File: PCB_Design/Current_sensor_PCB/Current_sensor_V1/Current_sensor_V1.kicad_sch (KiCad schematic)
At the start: 24 parts, among them J1 Screw_Terminal_01x02, J2 Barrel_Jack_MountingPin, J3 Conn_Coaxial, J4 Conn_Coaxial, J5 Conn_Coaxial, U1 CASR_6-NP

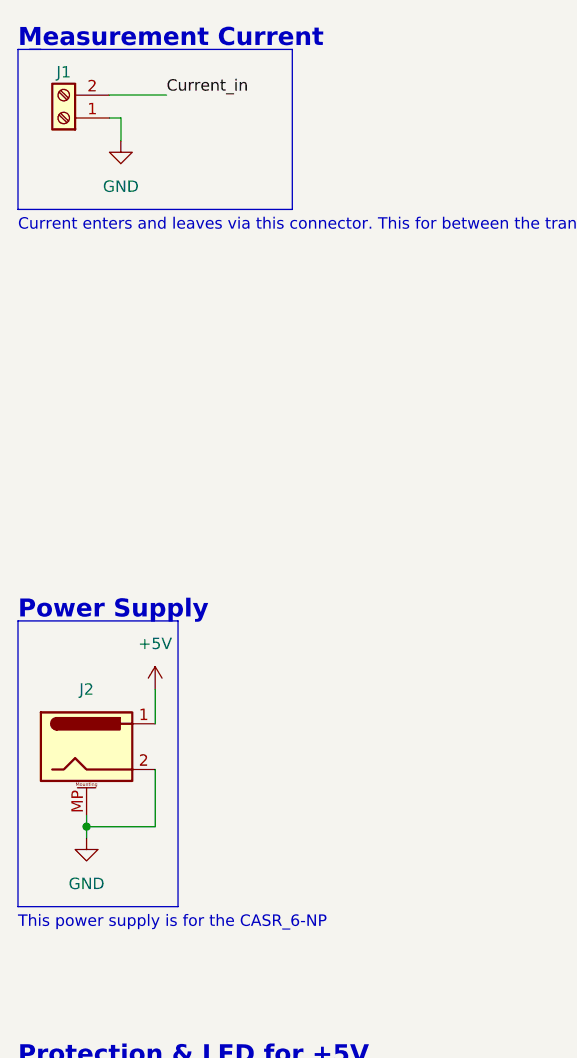
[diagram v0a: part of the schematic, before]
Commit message: Made Footprint and placed everything in the correct spot for Current V1
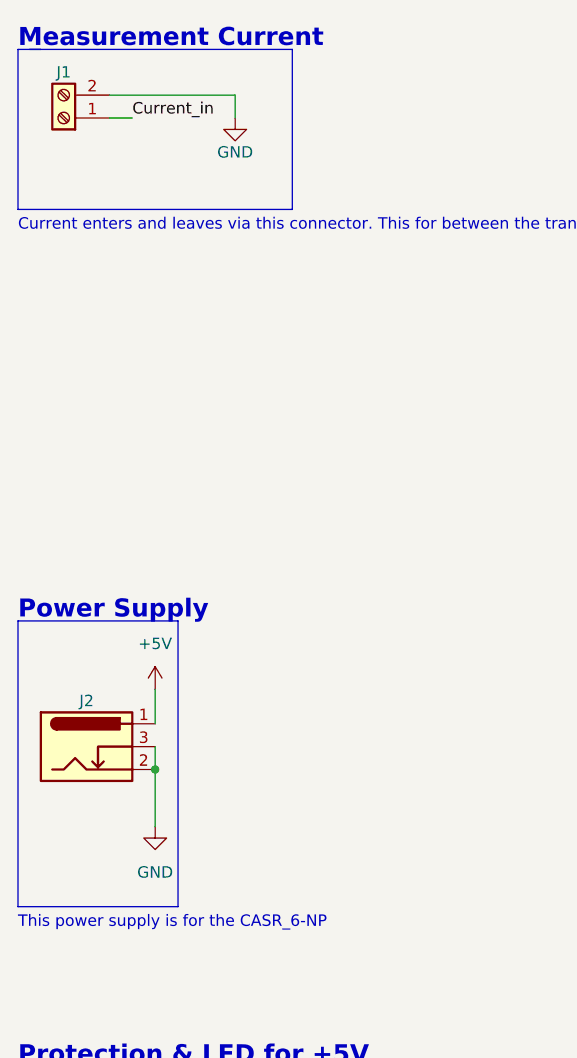
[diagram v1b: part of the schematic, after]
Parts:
- removed J2: Barrel_Jack_MountingPin, Connector_BarrelJack:BarrelJack_CLIFF_FC681465S_SMT_Horizontal, symbol Connector:Barrel_Jack_MountingPin
- added J2: Barrel_Jack_Switch, Connector_BarrelJack:BarrelJack_CLIFF_FC681465S_SMT_Horizontal, symbol Connector:Barrel_Jack_Switch
- J1: footprint (none) -> Custom_library:2_pin_terminal_block_socket
- R2: footprint (none) -> Custom_library:Shunt_Resistor
- U1: footprint (none) -> Custom_library:CASR6NP
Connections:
- net +5V: now also J2.1
- net Current_in: now also J1.1 (Pin_1); no longer J1.2 (Pin_2)
- net GND: now also J1.2 (Pin_2), J2.2, J2.3; no longer J1.1 (Pin_1)
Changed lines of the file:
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@@
   (junction (at 113.03 83.82) (diameter 0) (color 0 0 0 0)
   )
-  (junction (at 21.59 111.76) (diameter 0) (color 0 0 0 0)
-  )
   (junction (at 104.14 100.33) (diameter 0) (color 0 0 0 0)
   )
@@
   (junction (at 85.09 97.79) (diameter 0) (color 0 0 0 0)
   )
+  (junction (at 29.21 105.41) (diameter 0) (color 0 0 0 0)
+  )
   (wire (pts (xy 101.6 88.9) (xy 107.95 88.9))
     (stroke (width 0) (type default) (color 0 0 0 0))
@@
     (stroke (width 0) (type default) (color 0 0 0 0))
   )
-  (wire (pts (xy 25.4 35.56) (xy 25.4 33.02))
+  (wire (pts (xy 38.1 33.02) (xy 38.1 30.48))
     (stroke (width 0) (type default) (color 0 0 0 0))
   )
@@
     (stroke (width 0) (type default) (color 0 0 0 0))
   )
-  (wire (pts (xy 25.4 33.02) (xy 24.13 33.02))
-    (stroke (width 0) (type default) (color 0 0 0 0))
-  )
   (wire (pts (xy 26.67 156.21) (xy 26.67 157.48))
     (stroke (width 0) (type default) (color 0 0 0 0))
@@
     (stroke (width 0) (type default) (color 0 0 0 0))
   )
-  (wire (pts (xy 24.13 30.48) (xy 30.48 30.48))
-    (stroke (width 0) (type default) (color 0 0 0 0))
-  )
   (wire (pts (xy 231.14 97.79) (xy 234.95 97.79))
     (stroke (width 0) (type default) (color 0 0 0 0))
   )
+  (wire (pts (xy 24.13 33.02) (xy 26.67 33.02))
+    (stroke (width 0) (type default) (color 0 0 0 0))
+  )
   (wire (pts (xy 88.9 97.79) (xy 92.71 97.79))
     (stroke (width 0) (type default) (color 0 0 0 0))
@@
     (stroke (width 0) (type default) (color 0 0 0 0))
   )
-  (wire (pts (xy 21.59 110.49) (xy 21.59 111.76))
-    (stroke (width 0) (type default) (color 0 0 0 0))
-  )
   (wire (pts (xy 171.45 97.79) (xy 172.72 97.79))
     (stroke (width 0) (type default) (color 0 0 0 0))
@@
     (stroke (width 0) (type default) (color 0 0 0 0))
   )
+  (wire (pts (xy 24.13 30.48) (xy 38.1 30.48))
+    (stroke (width 0) (type default) (color 0 0 0 0))
+  )
   (wire (pts (xy 172.72 115.57) (xy 175.26 115.57))
     (stroke (width 0) (type default) (color 0 0 0 0))
@@
     (stroke (width 0) (type default) (color 0 0 0 0))
   )
-  (wire (pts (xy 21.59 111.76) (xy 21.59 113.03))
-    (stroke (width 0) (type default) (color 0 0 0 0))
-  )
   (wire (pts (xy 240.03 87.63) (xy 240.03 88.9))
     (stroke (width 0) (type default) (color 0 0 0 0))
@@
     (stroke (width 0) (type default) (color 0 0 0 0))
   )
-  (wire (pts (xy 21.59 111.76) (xy 29.21 111.76))
-    (stroke (width 0) (type default) (color 0 0 0 0))
-  )
   (wire (pts (xy 101.6 74.93) (xy 101.6 76.2))
+    (stroke (width 0) (type default) (color 0 0 0 0))
+  )
+  (wire (pts (xy 29.21 102.87) (xy 29.21 105.41))
     (stroke (width 0) (type default) (color 0 0 0 0))
   )
@@
     (effects (font (size 1.27 1.27)) (justify left bottom))
   )
-  (label "Current_in" (at 30.48 30.48 0)
+  (label "Current_in" (at 26.67 33.02 0)
     (effects (font (size 1.27 1.27)) (justify left bottom))
   )
@@
     (pin "2")
   )
-  (symbol (lib_id "power:GND") (at 25.4 35.56 0) (unit 1)
-    (in_bom yes) (on_board yes) (fields_autoplaced)
-    (property "Reference" "#PWR02" (id 0) (at 25.4 41.91 0)
-      (effects (font (size 1.27 1.27)) hide)
-    )
-    (property "Value" "GND" (id 1) (at 25.4 40.64 0))
-    (property "Footprint" "" (id 2) (at 25.4 35.56 0)
-      (effects (font (size 1.27 1.27)) hide)
-    )
-    (property "Datasheet" "" (id 3) (at 25.4 35.56 0)
+  (symbol (lib_id "power:GND") (at 38.1 33.02 0) (unit 1)
+    (in_bom yes) (on_board yes)
+    (property "Reference" "#PWR02" (id 0) (at 38.1 39.37 0)
+      (effects (font (size 1.27 1.27)) hide)
+    )
+    (property "Value" "GND" (id 1) (at 38.1 36.83 0))
+    (property "Footprint" "" (id 2) (at 38.1 33.02 0)
+      (effects (font (size 1.27 1.27)) hide)
+    )
+    (property "Datasheet" "" (id 3) (at 38.1 33.02 0)
       (effects (font (size 1.27 1.27)) hide)
     )
@@
       (effects (font (size 1.27 1.27)) (justify left))
     )
-    (property "Footprint" "" (id 2) (at 85.09 128.27 0)
+    (property "Footprint" "Custom_library:Shunt_Resistor" (id 2) (at 85.09 128.27 0)
       (effects (font (size 1.27 1.27)) hide)
     )
@@
     (pin "1")
   )
+  (symbol (lib_id "Connector:Barrel_Jack_Switch") (at 21.59 102.87 0) (unit 1)
+    (in_bom yes) (on_board yes)
+    (property "Reference" "J2" (id 0) (at 21.59 97.79 0))
+    (property "Value" "Barrel_Jack_Switch" (id 1) (at 21.59 96.52 0)
+      (effects (font (size 1.27 1.27)) hide)
+    )
+    (property "Footprint" "Connector_BarrelJack:BarrelJack_CLIFF_FC681465S_SMT_Horizontal" (id 2) (at 22.86 103.886 0)
+      (effects (font (size 1.27 1.27)) hide)
+    )
+    (property "Datasheet" "~" (id 3) (at 22.86 103.886 0)
+      (effects (font (size 1.27 1.27)) hide)
+    )
+    (pin "1")
+    (pin "2")
+    (pin "3")
+  )
   (symbol (lib_id "Device:R") (at 167.64 97.79 90) (unit 1)
     (in_bom yes) (on_board yes)
@@
       (effects (font (size 1.27 1.27)) (justify left))
     )
-    (property "Footprint" "" (id 2) (at 96.52 88.9 0)
+    (property "Footprint" "Custom_library:CASR6NP" (id 2) (at 96.52 88.9 0)
       (effects (font (size 1.27 1.27)) hide)
     )
@@
       (effects (font (size 1.27 1.27)) hide)
     )
-    (property "Footprint" "" (id 2) (at 19.05 33.02 0)
+    (property "Footprint" "Custom_library:2_pin_terminal_block_socket" (id 2) (at 19.05 33.02 0)
       (effects (font (size 1.27 1.27)) hide)
     )
@@
     (pin "2")
   )
-  (symbol (lib_id "Connector:Barrel_Jack_MountingPin") (at 21.59 102.87 0) (unit 1)
-    (in_bom yes) (on_board yes)
-    (property "Reference" "J2" (id 0) (at 21.59 96.52 0))
-    (property "Value" "Barrel_Jack_MountingPin" (id 1) (at 21.59 96.52 0)
-      (effects (font (size 1.27 1.27)) hide)
-    )
-    (property "Footprint" "Connector_BarrelJack:BarrelJack_CLIFF_FC681465S_SMT_Horizontal" (id 2) (at 22.86 103.886 0)
-      (effects (font (size 1.27 1.27)) hide)
-    )
-    (property "Datasheet" "~" (id 3) (at 22.86 103.886 0)
-      (effects (font (size 1.27 1.27)) hide)
-    )
-    (pin "1")
-    (pin "2")
-    (pin "MP")
-  )
-  (symbol (lib_id "power:GND") (at 21.59 113.03 0) (unit 1)
-    (in_bom yes) (on_board yes) (fields_autoplaced)
-    (property "Reference" "#PWR01" (id 0) (at 21.59 119.38 0)
-      (effects (font (size 1.27 1.27)) hide)
-    )
-    (property "Value" "GND" (id 1) (at 21.59 118.11 0))
-    (property "Footprint" "" (id 2) (at 21.59 113.03 0)
-      (effects (font (size 1.27 1.27)) hide)
-    )
-    (property "Datasheet" "" (id 3) (at 21.59 113.03 0)
+  (symbol (lib_id "power:GND") (at 29.21 111.76 0) (unit 1)
+    (in_bom yes) (on_board yes) (fields_autoplaced)
+    (property "Reference" "#PWR01" (id 0) (at 29.21 118.11 0)
+      (effects (font (size 1.27 1.27)) hide)
+    )
+    (property "Value" "GND" (id 1) (at 29.21 116.84 0))
+    (property "Footprint" "" (id 2) (at 29.21 111.76 0)
+      (effects (font (size 1.27 1.27)) hide)
+    )
+    (property "Datasheet" "" (id 3) (at 29.21 111.76 0)
       (effects (font (size 1.27 1.27)) hide)
     )
@@
     )
     (path "/d52b0ab5-3a89-4771-995d-e47e59ce23cb"
-      (reference "J1") (unit 1) (value "Screw_Terminal_01x02") (footprint "")
-    )
-    (path "/ecbf0ce9-6362-476e-9404-0953b2fd2000"
-      (reference "J2") (unit 1) (value "Barrel_Jack_MountingPin") (footprint "Connector_BarrelJack:BarrelJack_CLIFF_FC681465S_SMT_Horizontal")
+      (reference "J1") (unit 1) (value "Screw_Terminal_01x02") (footprint "Custom_library:2_pin_terminal_block_socket")
+    )
+    (path "/70f031d0-3eb7-4480-82bd-afe835fc105c"
+      (reference "J2") (unit 1) (value "Barrel_Jack_Switch") (footprint "Connector_BarrelJack:BarrelJack_CLIFF_FC681465S_SMT_Horizontal")
     )
     (path "/2a9c2945-d540-4fe5-8e72-b60a0f315ff9"
@@
     )
     (path "/39722ad3-e59e-4e7a-b786-b548a3fd9407"
-      (reference "R2") (unit 1) (value "OAR3 - R020FI") (footprint "")
+      (reference "R2") (unit 1) (value "OAR3 - R020FI") (footprint "Custom_library:Shunt_Resistor")
     )
     (path "/e0cfb964-8480-48ea-8177-6ad42931865f"
@@
     )
     (path "/98afcf01-8aa2-4880-a17b-690e52e479ba"
-      (reference "U1") (unit 1) (value "CASR_6-NP") (footprint "")
-    )
-  )
+      (reference "U1") (unit 1) (value "CASR_6-NP") (footprint "Custom_library:CASR6NP")
+    )
+  )

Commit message: Finished Current sensor V1 PCB
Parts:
- added H1, H2, H3, H4, H5: MountingHole, MountingHole:MountingHole_3.2mm_M3, symbol Mechanical:MountingHole
- J1: value Screw_Terminal_01x02 -> 284512-2
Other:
- note added: "Mounting Holes"
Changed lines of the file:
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@@
+    (stroke (width 0) (type default) (color 0 0 0 0))
+  )
+  (polyline (pts (xy 83.82 166.37) (xy 100.33 166.37))
     (stroke (width 0) (type default) (color 0 0 0 0))
   )
@@
     (stroke (width 0) (type default) (color 0 0 0 0))
   )
+  (polyline (pts (xy 100.33 166.37) (xy 100.33 184.15))
+    (stroke (width 0) (type default) (color 0 0 0 0))
+  )
   (wire (pts (xy 29.21 105.41) (xy 29.21 111.76))
     (stroke (width 0) (type default) (color 0 0 0 0))
@@
     (stroke (width 0) (type default) (color 0 0 0 0))
   )
+  (polyline (pts (xy 83.82 184.15) (xy 83.82 166.37))
+    (stroke (width 0) (type default) (color 0 0 0 0))
+  )
   (polyline (pts (xy 213.36 78.74) (xy 259.08 78.74))
     (stroke (width 0) (type default) (color 0 0 0 0))
@@
   )
   (wire (pts (xy 85.09 133.35) (xy 85.09 135.89))
+    (stroke (width 0) (type default) (color 0 0 0 0))
+  )
+  (polyline (pts (xy 100.33 184.15) (xy 83.82 184.15))
     (stroke (width 0) (type default) (color 0 0 0 0))
   )
@@
     (effects (font (size 2 2) (thickness 0.6) bold) (justify left bottom))
   )
+  (text "Mounting Holes\n" (at 83.82 166.37 0)
+    (effects (font (size 2 2) (thickness 0.6) bold) (justify left bottom))
+  )
   (text "For the CASR_6-NP V_Out needs a minimum load of 1k. V_Ref needs a maximum 1uF capacitor for filtering\n\n\n"
     (at 80.01 152.4 0)
@@
     (pin "1")
     (pin "2")
+  )
+  (symbol (lib_id "Mechanical:MountingHole") (at 93.98 176.53 0) (unit 1)
+    (in_bom yes) (on_board yes) (fields_autoplaced)
+    (property "Reference" "H5" (id 0) (at 96.52 175.2599 0)
+      (effects (font (size 1.27 1.27)) (justify left))
+    )
+    (property "Value" "MountingHole" (id 1) (at 96.52 177.7999 0)
+      (effects (font (size 1.27 1.27)) (justify left) hide)
+    )
+    (property "Footprint" "MountingHole:MountingHole_3.2mm_M3" (id 2) (at 93.98 176.53 0)
+      (effects (font (size 1.27 1.27)) hide)
+    )
+    (property "Datasheet" "~" (id 3) (at 93.98 176.53 0)
+      (effects (font (size 1.27 1.27)) hide)
+    )
   )
   (symbol (lib_id "power:GND") (at 240.03 104.14 0) (unit 1)
@@
     (pin "2")
   )
+  (symbol (lib_id "Mechanical:MountingHole") (at 86.36 170.18 0) (unit 1)
+    (in_bom yes) (on_board yes) (fields_autoplaced)
+    (property "Reference" "H1" (id 0) (at 88.9 168.9099 0)
+      (effects (font (size 1.27 1.27)) (justify left))
+    )
+    (property "Value" "MountingHole" (id 1) (at 88.9 171.4499 0)
+      (effects (font (size 1.27 1.27)) (justify left) hide)
+    )
+    (property "Footprint" "MountingHole:MountingHole_3.2mm_M3" (id 2) (at 86.36 170.18 0)
+      (effects (font (size 1.27 1.27)) hide)
+    )
+    (property "Datasheet" "~" (id 3) (at 86.36 170.18 0)
+      (effects (font (size 1.27 1.27)) hide)
+    )
+  )
   (symbol (lib_id "power:GND") (at 85.09 135.89 0) (unit 1)
     (in_bom yes) (on_board yes) (fields_autoplaced)
@@
     (pin "1")
     (pin "2")
+  )
+  (symbol (lib_id "Mechanical:MountingHole") (at 86.36 181.61 0) (unit 1)
+    (in_bom yes) (on_board yes) (fields_autoplaced)
+    (property "Reference" "H3" (id 0) (at 88.9 180.3399 0)
+      (effects (font (size 1.27 1.27)) (justify left))
+    )
+    (property "Value" "MountingHole" (id 1) (at 88.9 182.8799 0)
+      (effects (font (size 1.27 1.27)) (justify left) hide)
+    )
+    (property "Footprint" "MountingHole:MountingHole_3.2mm_M3" (id 2) (at 86.36 181.61 0)
+      (effects (font (size 1.27 1.27)) hide)
+    )
+    (property "Datasheet" "~" (id 3) (at 86.36 181.61 0)
+      (effects (font (size 1.27 1.27)) hide)
+    )
   )
   (symbol (lib_id "Custom_library:CASR_6-NP") (at 96.52 88.9 0) (mirror y) (unit 1)
@@
     (pin "2")
   )
+  (symbol (lib_id "Mechanical:MountingHole") (at 86.36 176.53 0) (unit 1)
+    (in_bom yes) (on_board yes) (fields_autoplaced)
+    (property "Reference" "H2" (id 0) (at 88.9 175.2599 0)
+      (effects (font (size 1.27 1.27)) (justify left))
+    )
+    (property "Value" "MountingHole" (id 1) (at 88.9 177.7999 0)
+      (effects (font (size 1.27 1.27)) (justify left) hide)
+    )
+    (property "Footprint" "MountingHole:MountingHole_3.2mm_M3" (id 2) (at 86.36 176.53 0)
+      (effects (font (size 1.27 1.27)) hide)
+    )
+    (property "Datasheet" "~" (id 3) (at 86.36 176.53 0)
+      (effects (font (size 1.27 1.27)) hide)
+    )
+  )
   (symbol (lib_id "Device:R") (at 107.95 92.71 180) (unit 1)
     (in_bom yes) (on_board yes)
@@
     (in_bom yes) (on_board yes)
     (property "Reference" "J1" (id 0) (at 19.05 27.94 0))
-    (property "Value" "Screw_Terminal_01x02" (id 1) (at 19.05 26.67 0)
+    (property "Value" "284512-2" (id 1) (at 19.05 26.67 0)
       (effects (font (size 1.27 1.27)) hide)
     )
@@
     (pin "2")
   )
+  (symbol (lib_id "Mechanical:MountingHole") (at 93.98 170.18 0) (unit 1)
+    (in_bom yes) (on_board yes) (fields_autoplaced)
+    (property "Reference" "H4" (id 0) (at 96.52 168.9099 0)
+      (effects (font (size 1.27 1.27)) (justify left))
+    )
+    (property "Value" "MountingHole" (id 1) (at 96.52 171.4499 0)
+      (effects (font (size 1.27 1.27)) (justify left) hide)
+    )
+    (property "Footprint" "MountingHole:MountingHole_3.2mm_M3" (id 2) (at 93.98 170.18 0)
+      (effects (font (size 1.27 1.27)) hide)
+    )
+    (property "Datasheet" "~" (id 3) (at 93.98 170.18 0)
+      (effects (font (size 1.27 1.27)) hide)
+    )
+  )
   (symbol (lib_id "power:GND") (at 29.21 111.76 0) (unit 1)
     (in_bom yes) (on_board yes) (fields_autoplaced)
@@
       (reference "D2") (unit 1) (value "GREEN") (footprint "Diode_SMD:D_1206_3216Metric")
     )
+    (path "/63254d89-b1fe-4890-8526-4ad04937db25"
+      (reference "H1") (unit 1) (value "MountingHole") (footprint "MountingHole:MountingHole_3.2mm_M3")
+    )
+    (path "/ac17a04a-b5c8-4147-884b-dee08aebd4fd"
+      (reference "H2") (unit 1) (value "MountingHole") (footprint "MountingHole:MountingHole_3.2mm_M3")
+    )
+    (path "/8c78091d-dbc5-4103-94a4-2d125426e342"
+      (reference "H3") (unit 1) (value "MountingHole") (footprint "MountingHole:MountingHole_3.2mm_M3")
+    )
+    (path "/f563e275-b15d-4c24-a871-db07a0c8a140"
+      (reference "H4") (unit 1) (value "MountingHole") (footprint "MountingHole:MountingHole_3.2mm_M3")
+    )
+    (path "/417e9dd0-cacb-4791-9f41-9eff92cd143b"
+      (reference "H5") (unit 1) (value "MountingHole") (footprint "MountingHole:MountingHole_3.2mm_M3")
+    )
     (path "/d52b0ab5-3a89-4771-995d-e47e59ce23cb"
-      (reference "J1") (unit 1) (value "Screw_Terminal_01x02") (footprint "Custom_library:2_pin_terminal_block_socket")
+      (reference "J1") (unit 1) (value "284512-2") (footprint "Custom_library:2_pin_terminal_block_socket")
     )
     (path "/70f031d0-3eb7-4480-82bd-afe835fc105c"
